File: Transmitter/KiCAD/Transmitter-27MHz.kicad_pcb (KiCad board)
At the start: 2 copper layers, 63.5 x 54.5 mm, 24 parts, among them J1 PRPC040SACN-RC, J2 PRPC040SACN-RC, Q700 S8550, Q701 2N3904, Q702 2N3904, Q703 2N3904, U1 COP411, Y700 455KHz

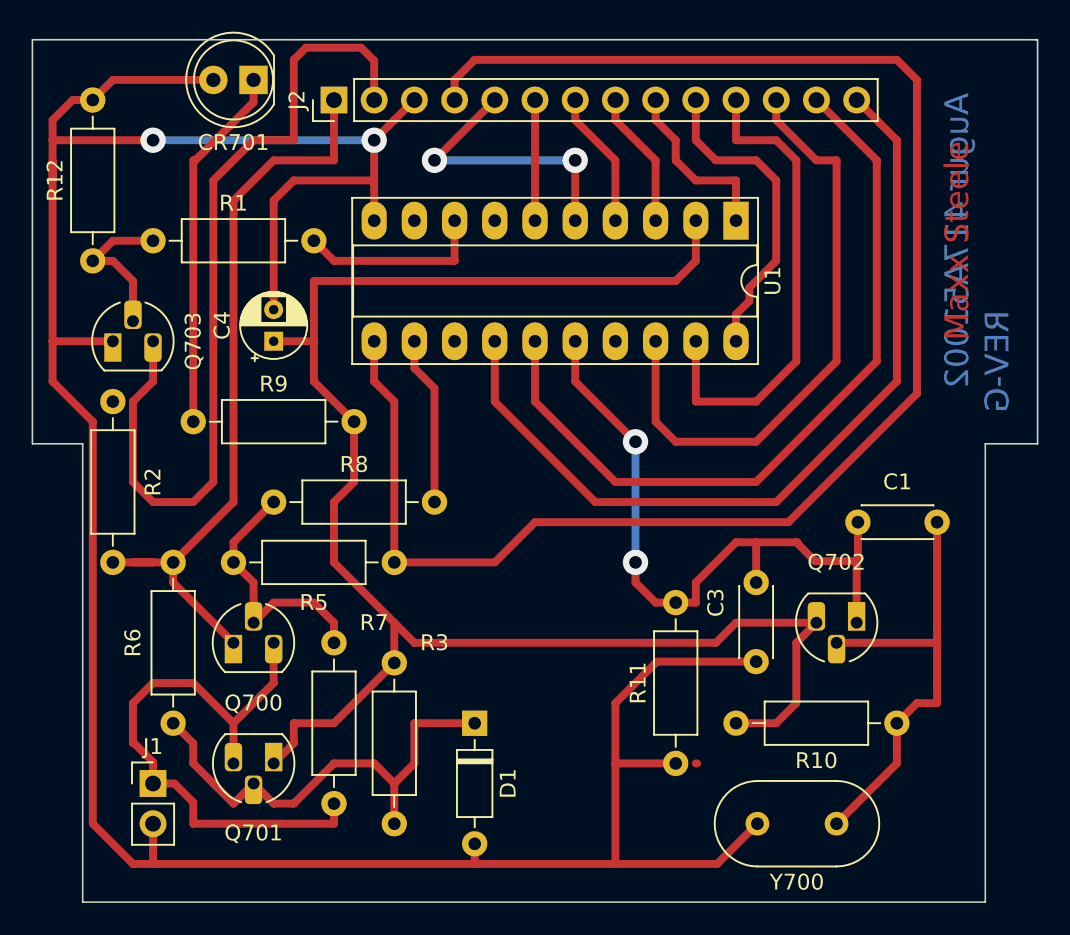
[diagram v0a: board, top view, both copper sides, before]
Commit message: Upgrade legacy KiCad schematics to KiCad 10 native format
- Add tools/upgrade_legacy_sch.py to convert EESchema v4 .sch to .kicad_sch + .kicad_pro
- Upgrade Transmitter and Receiver projects with embedded symbols and exported PDFs
- Upgrade Transmitter PCB to KiCad 10 format via kicad-cli pcb upgrade
- Add cop41xl.kicad_sym (upgraded from legacy cop41xl.lib) and update all sym-lib-table entries
- Document KiCad 10 open instructions in Transmitter/KiCAD and Receiver/KiCAD READMEs
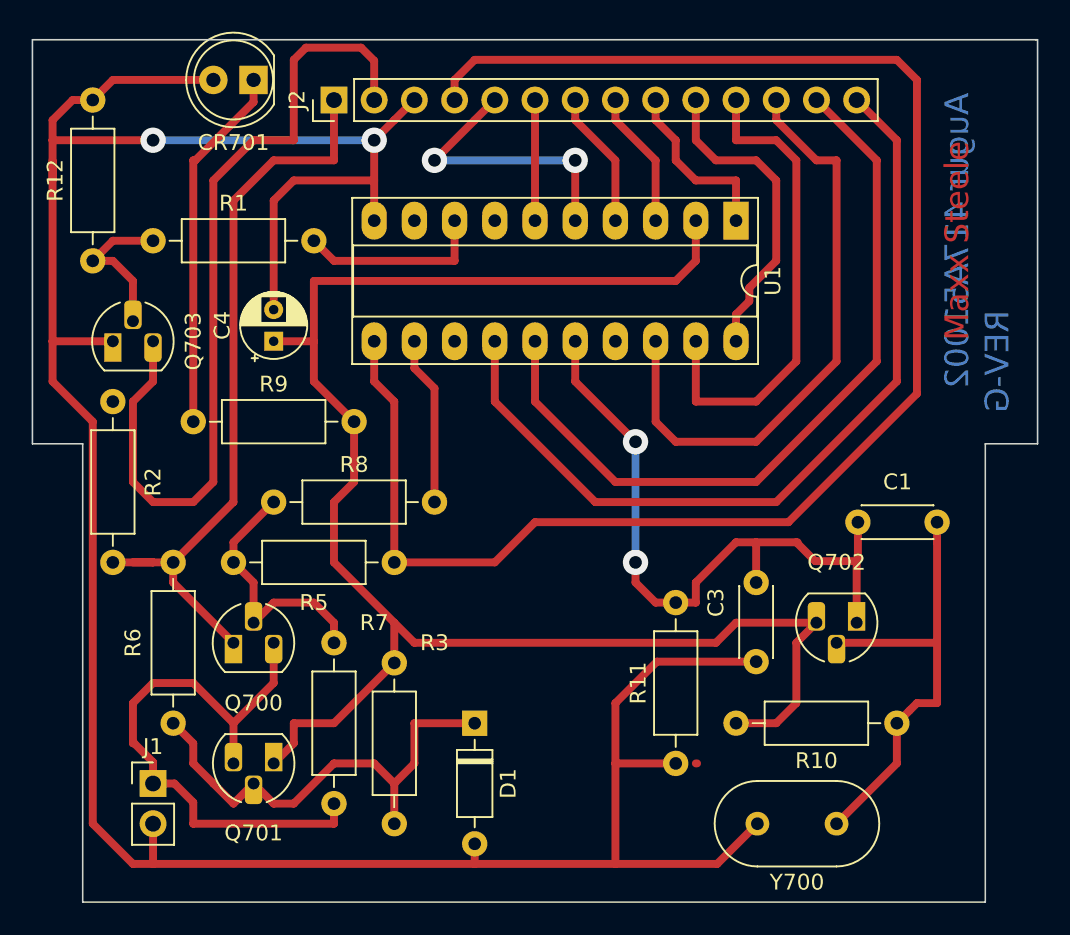
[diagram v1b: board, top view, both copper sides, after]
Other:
- net class Default removed
